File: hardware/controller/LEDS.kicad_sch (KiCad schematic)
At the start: 21 parts, among them IC901 PCA9685PW_Q900,118, Q901 IRLML6402TRPBF, Q902 IRLML6402TRPBF

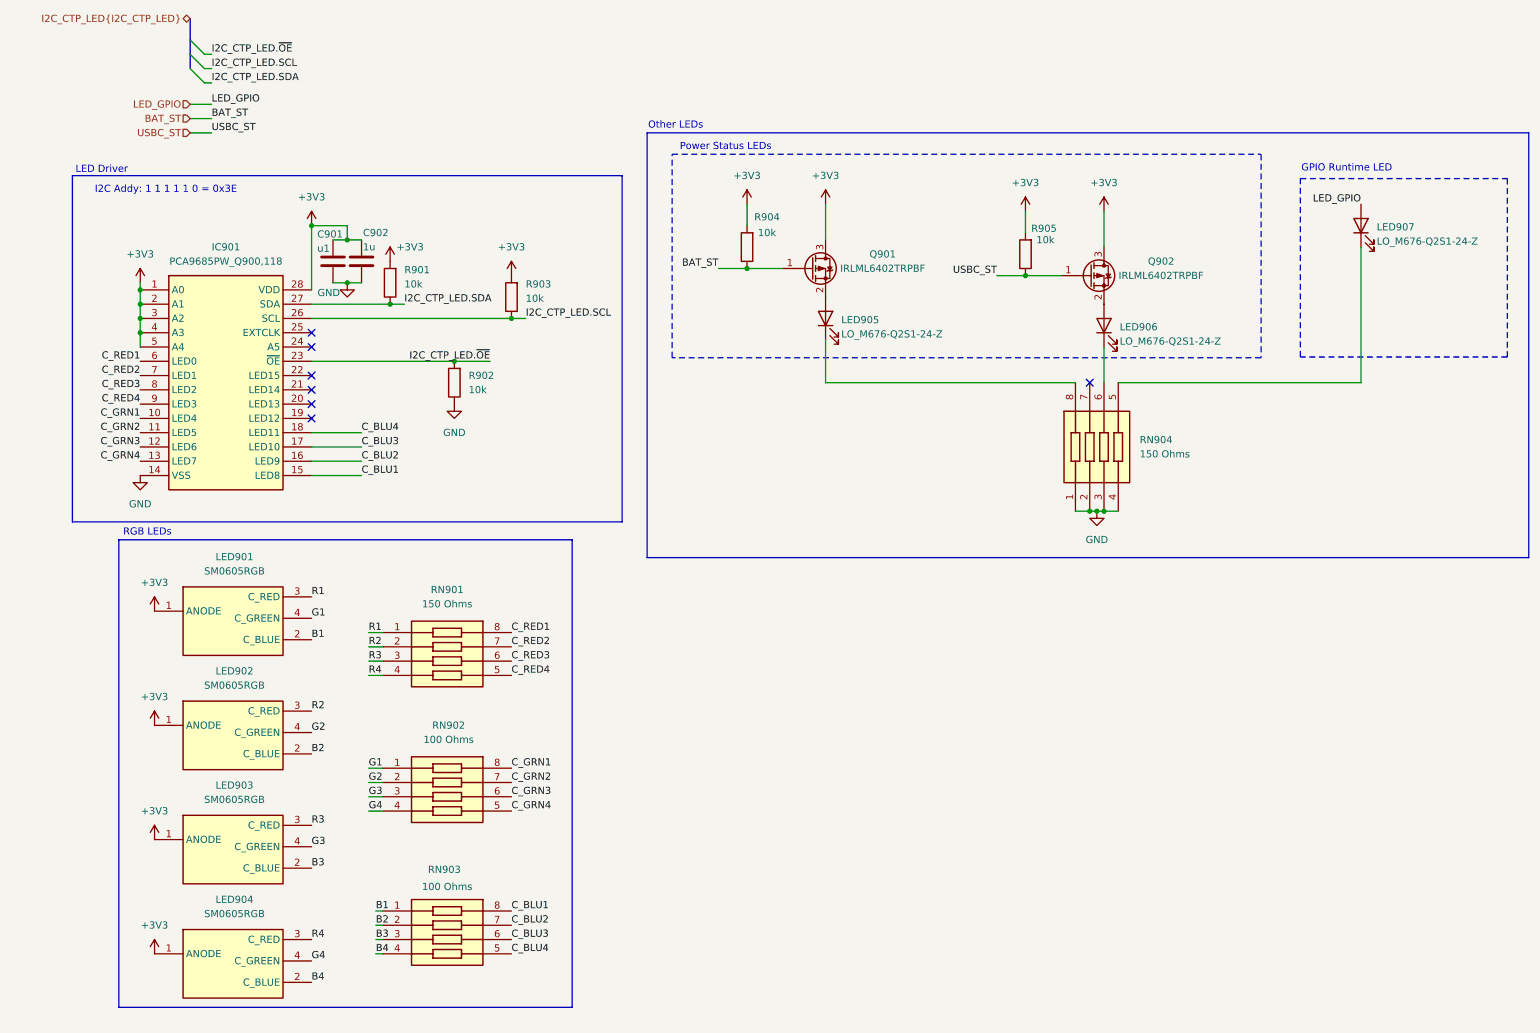
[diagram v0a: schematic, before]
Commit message: fixed 3d models. rounded edges of pcb
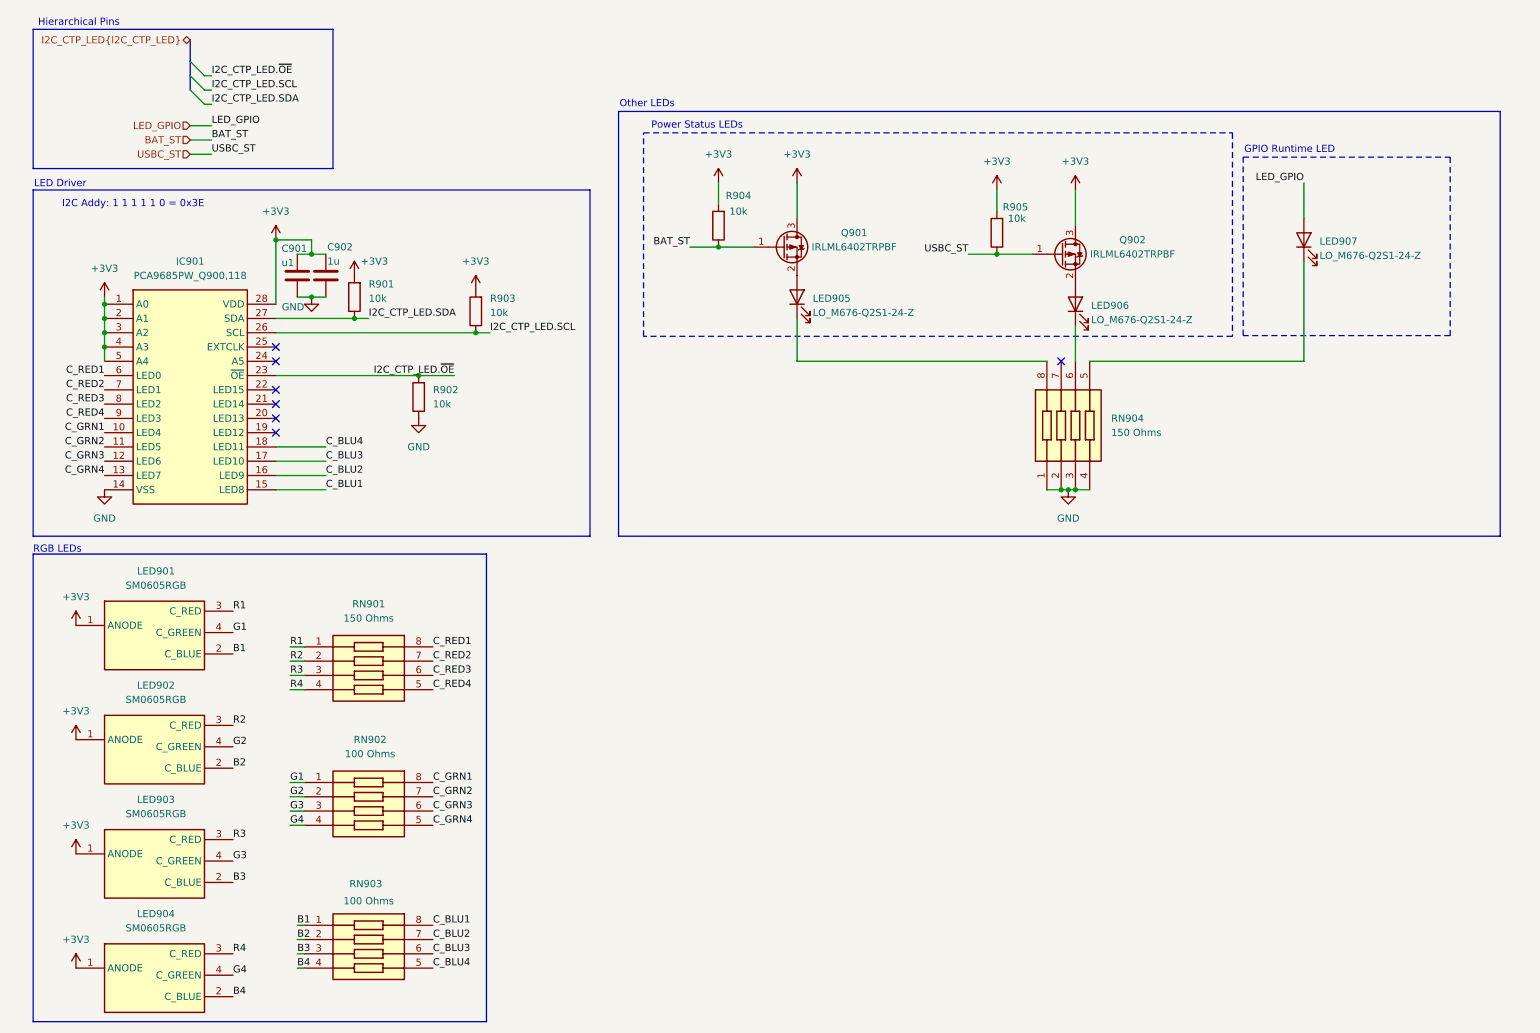
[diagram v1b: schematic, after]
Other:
- note added: "Hierarchical Pins"
- moved on the sheet: C901, C902, IC901, LED901, LED902, LED903, LED904, LED905, LED906, LED907, Q901, Q902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

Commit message: a
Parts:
- R901, R902, R903, R904, R905: footprint SamacSys_Parts:RESC2012X60N -> RESC2012X60N
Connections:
- net +3V3: now also R902.1
- net C_BLU1: now also IC901.6 (LED0); no longer IC901.15 (LED8)
- net C_BLU2: now also IC901.7 (LED1); no longer IC901.16 (LED9)
- net C_BLU3: now also IC901.8 (LED2); no longer IC901.17 (LED10)
- net C_BLU4: now also IC901.9 (LED3); no longer IC901.18 (LED11)
- net C_GRN1: now also IC901.18 (LED11); no longer IC901.10 (LED4)
- net C_GRN2: now also IC901.17 (LED10); no longer IC901.11 (LED5)
- net C_GRN3: now also IC901.16 (LED9); no longer IC901.12 (LED6)
- net C_GRN4: now also IC901.15 (LED8); no longer IC901.13 (LED7)
- net C_RED1: now also IC901.10 (LED4); no longer IC901.6 (LED0)
- net C_RED2: now also IC901.11 (LED5); no longer IC901.7 (LED1)
- net C_RED3: now also IC901.12 (LED6); no longer IC901.8 (LED2)
- net C_RED4: now also IC901.13 (LED7); no longer IC901.9 (LED3)
- net GND: no longer R902.1
- net at LED907.1 (K): now also RN904.8; no longer RN904.5
- net at LED905.1 (K): now also RN904.5; no longer RN904.8
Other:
- moved on the sheet: LED905, LED906, LED907, Q901, Q902, R902, R904, R905, RN904

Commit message: save before nuke
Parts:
- R121: renamed from R901; footprint RESC2012X60N -> SamacSys_Parts:RESC2012X60N
- R122: renamed from R903; footprint RESC2012X60N -> SamacSys_Parts:RESC2012X60N
- R123: renamed from R902; footprint RESC2012X60N -> SamacSys_Parts:RESC2012X60N
- R124: renamed from R904; footprint RESC2012X60N -> SamacSys_Parts:RESC2012X60N
- R125: renamed from R905; footprint RESC2012X60N -> SamacSys_Parts:RESC2012X60N
- renumbered C901 to C123, C902 to C124, IC901 to IC105, LED901 to LED101, LED902 to LED102, LED903 to LED103, LED904 to LED104, LED905 to LED105, LED906 to LED106, LED907 to LED107, Q901 to Q103, Q902 to Q104, RN901 to RN101, RN902 to RN102, RN903 to RN103, RN904 to RN104

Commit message: done but need to add stitching vias
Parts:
- LED905: renamed from LED105; Function (none) -> BAT_ST
- LED906: renamed from LED106; Function (none) -> USBC_ST
- LED907: renamed from LED107; Function (none) -> LED_GPIO
- renumbered C123 to C901, C124 to C902, IC105 to IC901, LED101 to LED901, LED102 to LED902, LED103 to LED903, LED104 to LED904, Q103 to Q901, Q104 to Q902, R121 to R901, R122 to R902, R123 to R903, R124 to R904, R125 to R905, RN101 to RN901, RN102 to RN902, RN103 to RN903, RN104 to RN904

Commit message: forgor
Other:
- note added: "RGB LED Driver"
- note removed: "LED Driver"
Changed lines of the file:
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@@
+	)
+	(rectangle
+		(start 15.24 45.72)
+		(end 123.19 105.918)
+		(stroke
+			(width 0)
+			(type default)
+		)
+		(fill
+			(type none)
+		)
 	)
 	(rectangle
@@
 		)
 	)
-	(text "LED Driver"
+	(text "RGB LED Driver"
 		(exclude_from_sim no)
-		(at 20.066 44.704 0)
+		(at 22.352 44.704 0)
 		(effects
 			(font

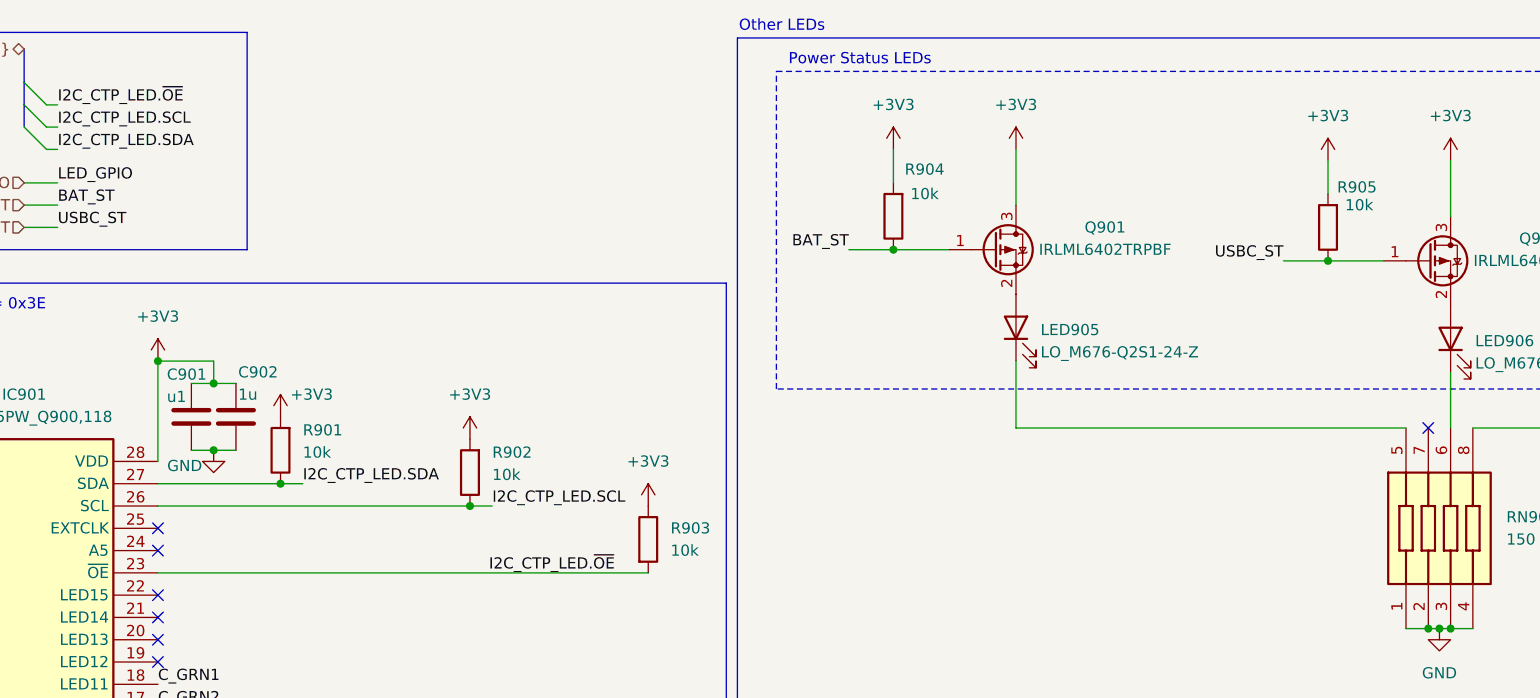
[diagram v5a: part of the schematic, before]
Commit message: clean up DRC. need to add stitching vias and figure out why inner ground plane isnt connected to F.Cu pour
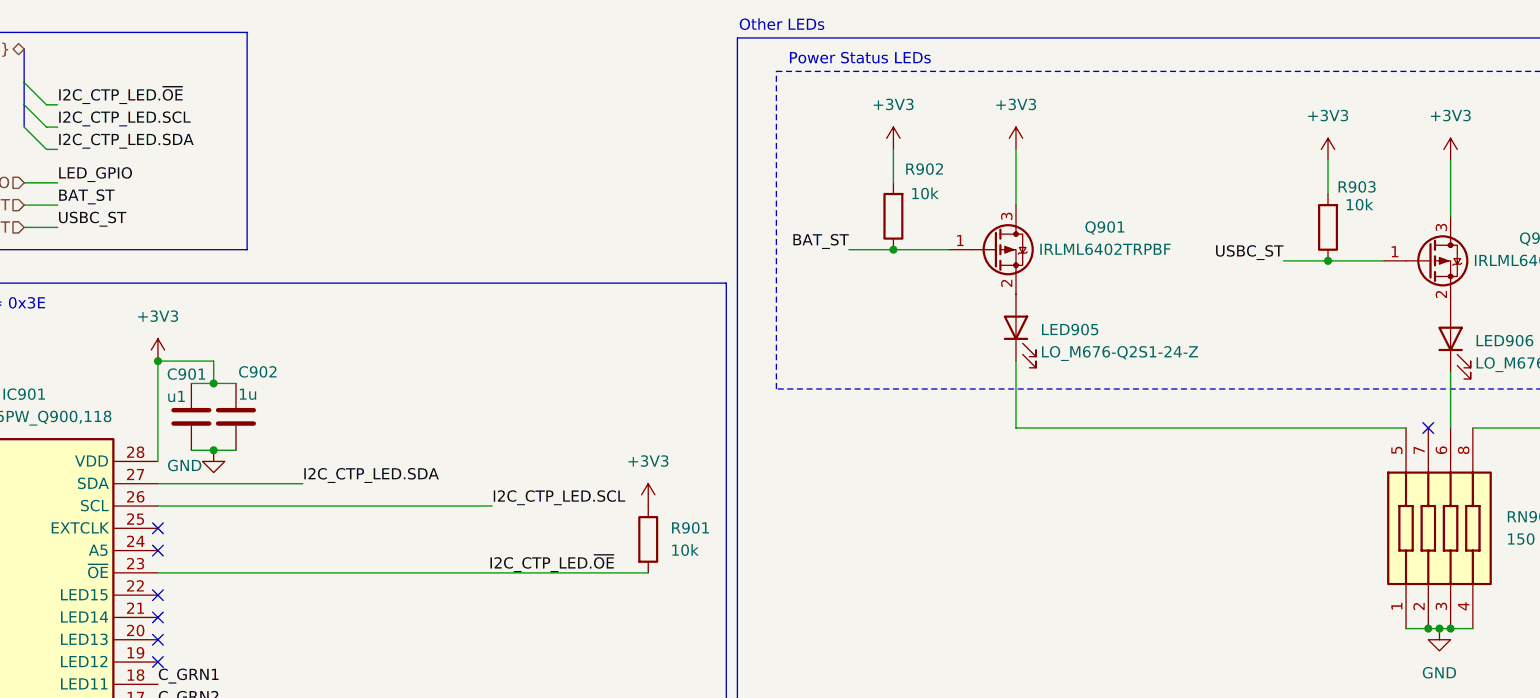
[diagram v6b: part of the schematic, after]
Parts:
- removed R901, R902: 10k, SamacSys_Parts:RESC2012X60N, symbol Device:R
- renumbered R903 to R901, R904 to R902, R905 to R903
